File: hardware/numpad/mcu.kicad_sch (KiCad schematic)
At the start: 9 parts, among them U1 STM32L011F4Px

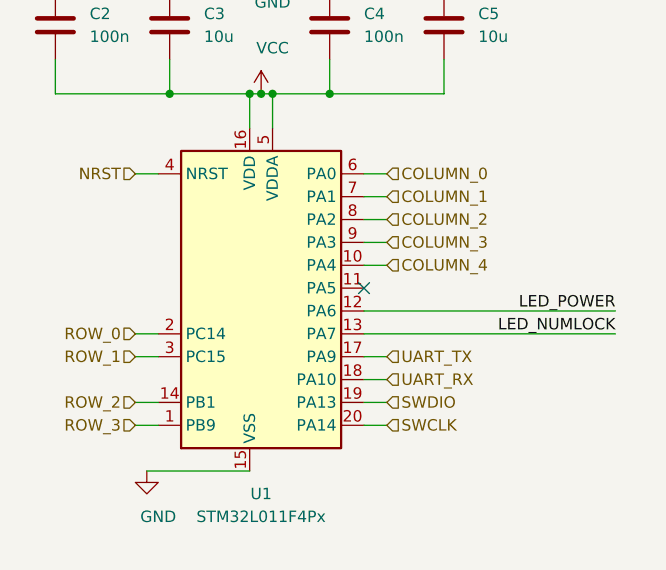
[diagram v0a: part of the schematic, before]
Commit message: Numpad: Fix labels of columns and rows of the key matrix
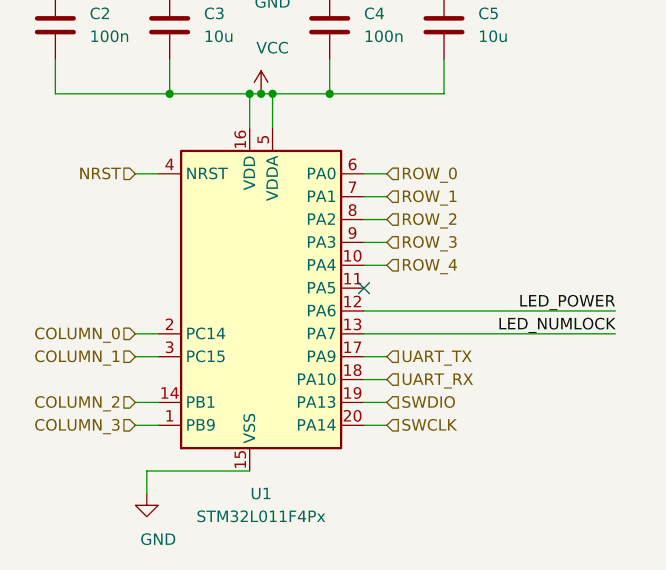
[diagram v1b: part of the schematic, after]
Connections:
- net COLUMN_0: now also U1.2 (PC14); no longer U1.6 (PA0)
- net COLUMN_1: now also U1.3 (PC15); no longer U1.7 (PA1)
- net COLUMN_2: now also U1.14 (PB1); no longer U1.8 (PA2)
- net COLUMN_3: now also U1.1 (PB9); no longer U1.9 (PA3)
- net ROW_0: now also U1.6 (PA0); no longer U1.2 (PC14)
- net ROW_1: now also U1.7 (PA1); no longer U1.3 (PC15)
- net ROW_2: now also U1.8 (PA2); no longer U1.14 (PB1)
- net ROW_3: now also U1.9 (PA3); no longer U1.1 (PB9)
- net COLUMN_4 renamed ROW_4
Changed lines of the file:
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@@
+    (stroke (width 0) (type solid) (color 0 0 0 0))
+  )
+  (wire (pts (xy 90.17 123.19) (xy 90.17 125.73))
     (stroke (width 0) (type solid) (color 0 0 0 0))
   )
@@
     (effects (font (size 1.27 1.27)) (justify right))
   )
-  (hierarchical_label "ROW_0" (shape input) (at 88.9 107.95 180)
+  (hierarchical_label "COLUMN_0" (shape input) (at 88.9 107.95 180)
     (effects (font (size 1.27 1.27)) (justify right))
   )
-  (hierarchical_label "ROW_1" (shape input) (at 88.9 110.49 180)
+  (hierarchical_label "COLUMN_1" (shape input) (at 88.9 110.49 180)
     (effects (font (size 1.27 1.27)) (justify right))
   )
-  (hierarchical_label "ROW_2" (shape input) (at 88.9 115.57 180)
+  (hierarchical_label "COLUMN_2" (shape input) (at 88.9 115.57 180)
     (effects (font (size 1.27 1.27)) (justify right))
   )
-  (hierarchical_label "ROW_3" (shape input) (at 88.9 118.11 180)
+  (hierarchical_label "COLUMN_3" (shape input) (at 88.9 118.11 180)
     (effects (font (size 1.27 1.27)) (justify right))
   )
-  (hierarchical_label "COLUMN_0" (shape input) (at 116.84 90.17 0)
+  (hierarchical_label "ROW_0" (shape input) (at 116.84 90.17 0)
     (effects (font (size 1.27 1.27)) (justify left))
   )
-  (hierarchical_label "COLUMN_1" (shape input) (at 116.84 92.71 0)
+  (hierarchical_label "ROW_1" (shape input) (at 116.84 92.71 0)
     (effects (font (size 1.27 1.27)) (justify left))
   )
-  (hierarchical_label "COLUMN_2" (shape input) (at 116.84 95.25 0)
+  (hierarchical_label "ROW_2" (shape input) (at 116.84 95.25 0)
     (effects (font (size 1.27 1.27)) (justify left))
   )
-  (hierarchical_label "COLUMN_3" (shape input) (at 116.84 97.79 0)
+  (hierarchical_label "ROW_3" (shape input) (at 116.84 97.79 0)
     (effects (font (size 1.27 1.27)) (justify left))
   )
-  (hierarchical_label "COLUMN_4" (shape input) (at 116.84 100.33 0)
+  (hierarchical_label "ROW_4" (shape input) (at 116.84 100.33 0)
     (effects (font (size 1.27 1.27)) (justify left))
   )
@@
     (pin "1")
   )
-  (symbol (lib_id "power:GND") (at 90.17 123.19 0) (unit 1)
+  (symbol (lib_id "power:GND") (at 90.17 125.73 0) (unit 1)
     (in_bom yes) (on_board yes)
-    (property "Reference" "#PWR0111" (id 0) (at 90.17 129.54 0)
+    (property "Reference" "#PWR0111" (id 0) (at 90.17 132.08 0)
       (effects (font (size 1.27 1.27)) hide)
     )
-    (property "Value" "GND" (id 1) (at 91.44 128.27 0))
-    (property "Footprint" "" (id 2) (at 90.17 123.19 0)
+    (property "Value" "GND" (id 1) (at 91.44 130.81 0))
+    (property "Footprint" "" (id 2) (at 90.17 125.73 0)
       (effects (font (size 1.27 1.27)) hide)
     )
-    (property "Datasheet" "" (id 3) (at 90.17 123.19 0)
+    (property "Datasheet" "" (id 3) (at 90.17 125.73 0)
       (effects (font (size 1.27 1.27)) hide)
     )

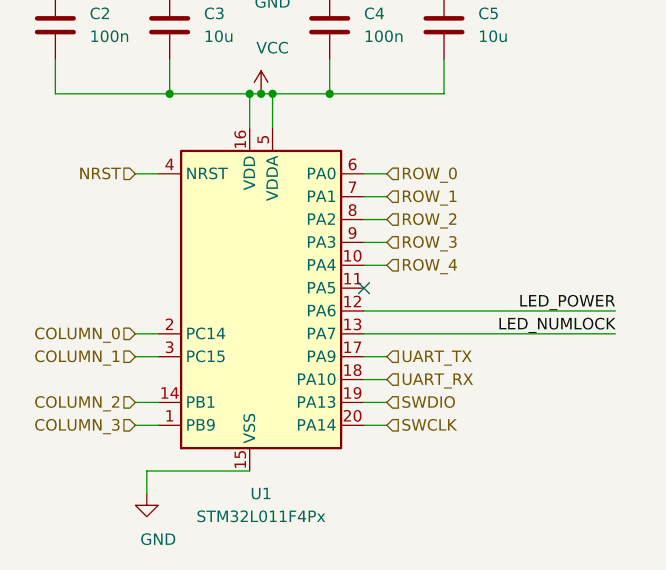
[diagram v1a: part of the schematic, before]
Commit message: Numpad: Create traces from the MCU to the keymatrix
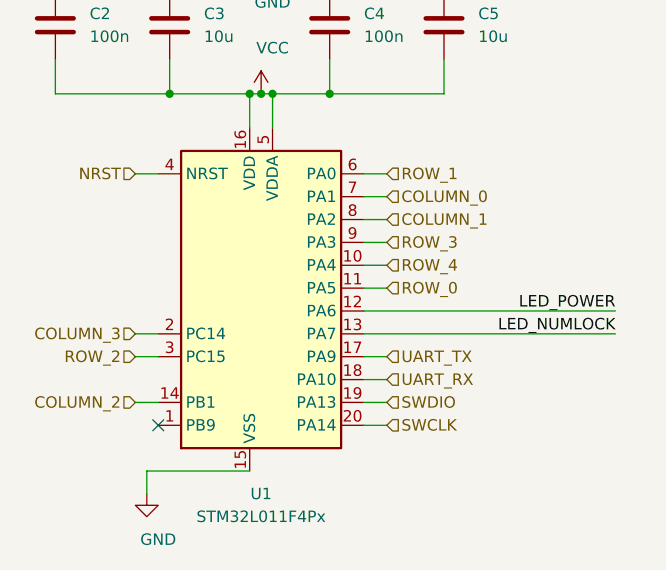
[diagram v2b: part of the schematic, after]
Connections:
- net COLUMN_0: now also U1.7 (PA1); no longer U1.2 (PC14)
- net COLUMN_1: now also U1.8 (PA2); no longer U1.3 (PC15)
- net COLUMN_3: now also U1.2 (PC14); no longer U1.1 (PB9)
- net ROW_0: now also U1.11 (PA5); no longer U1.6 (PA0)
- net ROW_1: now also U1.6 (PA0); no longer U1.7 (PA1)
- net ROW_2: now also U1.3 (PC15); no longer U1.8 (PA2)
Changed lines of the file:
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@@
   (junction (at 110.49 81.28) (diameter 0.9144) (color 0 0 0 0))
   (junction (at 234.95 66.04) (diameter 0.9144) (color 0 0 0 0))
-  (no_connect (at 114.3 102.87))
+  (no_connect (at 91.44 118.11))
   (wire (pts (xy 80.01 66.04) (xy 80.01 69.85))
     (stroke (width 0) (type solid) (color 0 0 0 0))
@@
   )
   (wire (pts (xy 88.9 115.57) (xy 91.44 115.57))
-    (stroke (width 0) (type solid) (color 0 0 0 0))
-  )
-  (wire (pts (xy 88.9 118.11) (xy 91.44 118.11))
     (stroke (width 0) (type solid) (color 0 0 0 0))
   )
@@
     (stroke (width 0) (type solid) (color 0 0 0 0))
   )
+  (wire (pts (xy 116.84 102.87) (xy 114.3 102.87))
+    (stroke (width 0) (type solid) (color 0 0 0 0))
+  )
   (wire (pts (xy 123.19 66.04) (xy 123.19 69.85))
     (stroke (width 0) (type solid) (color 0 0 0 0))
@@
     (effects (font (size 1.27 1.27)) (justify right))
   )
-  (hierarchical_label "COLUMN_0" (shape input) (at 88.9 107.95 180)
+  (hierarchical_label "COLUMN_3" (shape input) (at 88.9 107.95 180)
     (effects (font (size 1.27 1.27)) (justify right))
   )
-  (hierarchical_label "COLUMN_1" (shape input) (at 88.9 110.49 180)
+  (hierarchical_label "ROW_2" (shape input) (at 88.9 110.49 180)
     (effects (font (size 1.27 1.27)) (justify right))
   )
@@
     (effects (font (size 1.27 1.27)) (justify right))
   )
-  (hierarchical_label "COLUMN_3" (shape input) (at 88.9 118.11 180)
-    (effects (font (size 1.27 1.27)) (justify right))
-  )
-  (hierarchical_label "ROW_0" (shape input) (at 116.84 90.17 0)
+  (hierarchical_label "ROW_1" (shape input) (at 116.84 90.17 0)
     (effects (font (size 1.27 1.27)) (justify left))
   )
-  (hierarchical_label "ROW_1" (shape input) (at 116.84 92.71 0)
+  (hierarchical_label "COLUMN_0" (shape input) (at 116.84 92.71 0)
     (effects (font (size 1.27 1.27)) (justify left))
   )
-  (hierarchical_label "ROW_2" (shape input) (at 116.84 95.25 0)
+  (hierarchical_label "COLUMN_1" (shape input) (at 116.84 95.25 0)
     (effects (font (size 1.27 1.27)) (justify left))
   )
@@
     (effects (font (size 1.27 1.27)) (justify left))
   )
+  (hierarchical_label "ROW_0" (shape input) (at 116.84 102.87 0)
+    (effects (font (size 1.27 1.27)) (justify left))
+  )

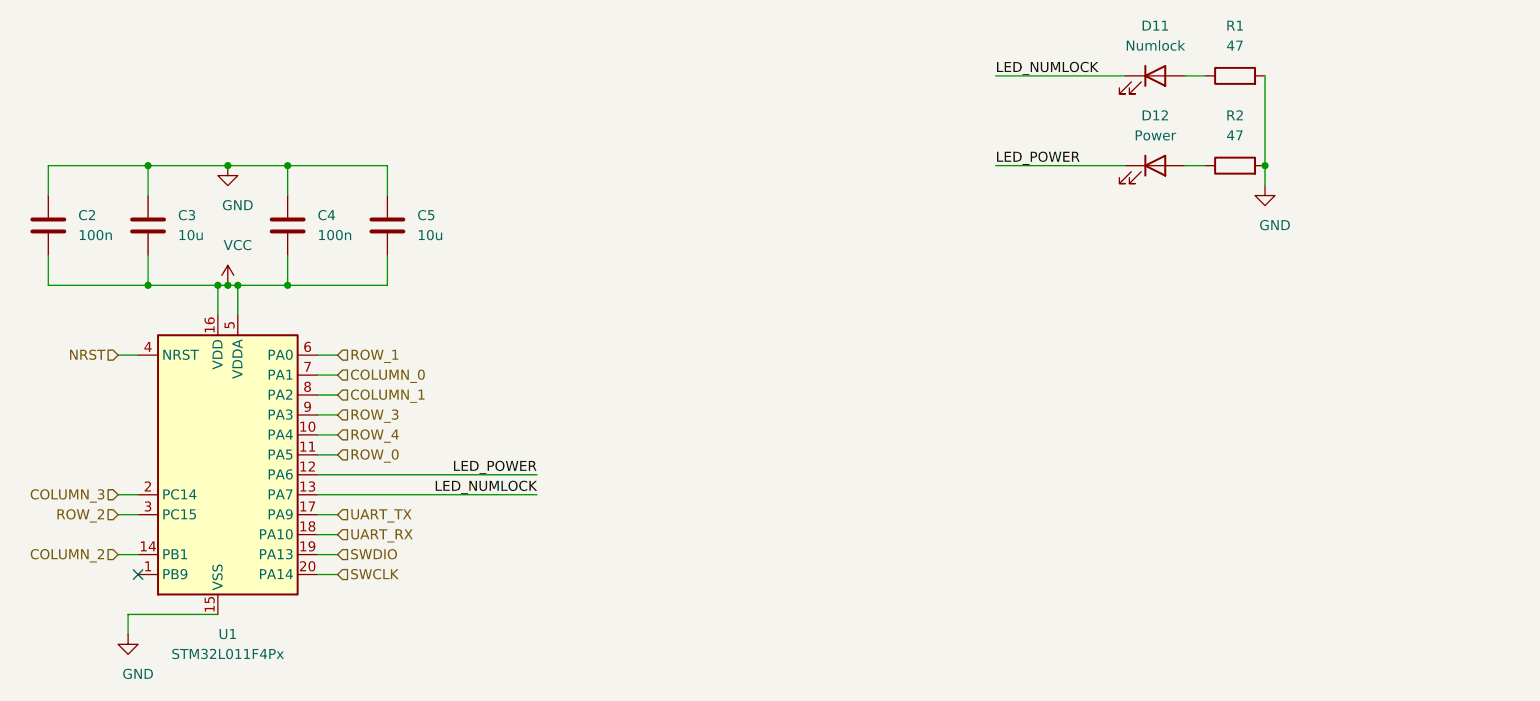
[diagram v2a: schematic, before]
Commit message: Numpad: Rework PCB layout
The Power-LED was eliminated and the Numpad-LED moved off the board.
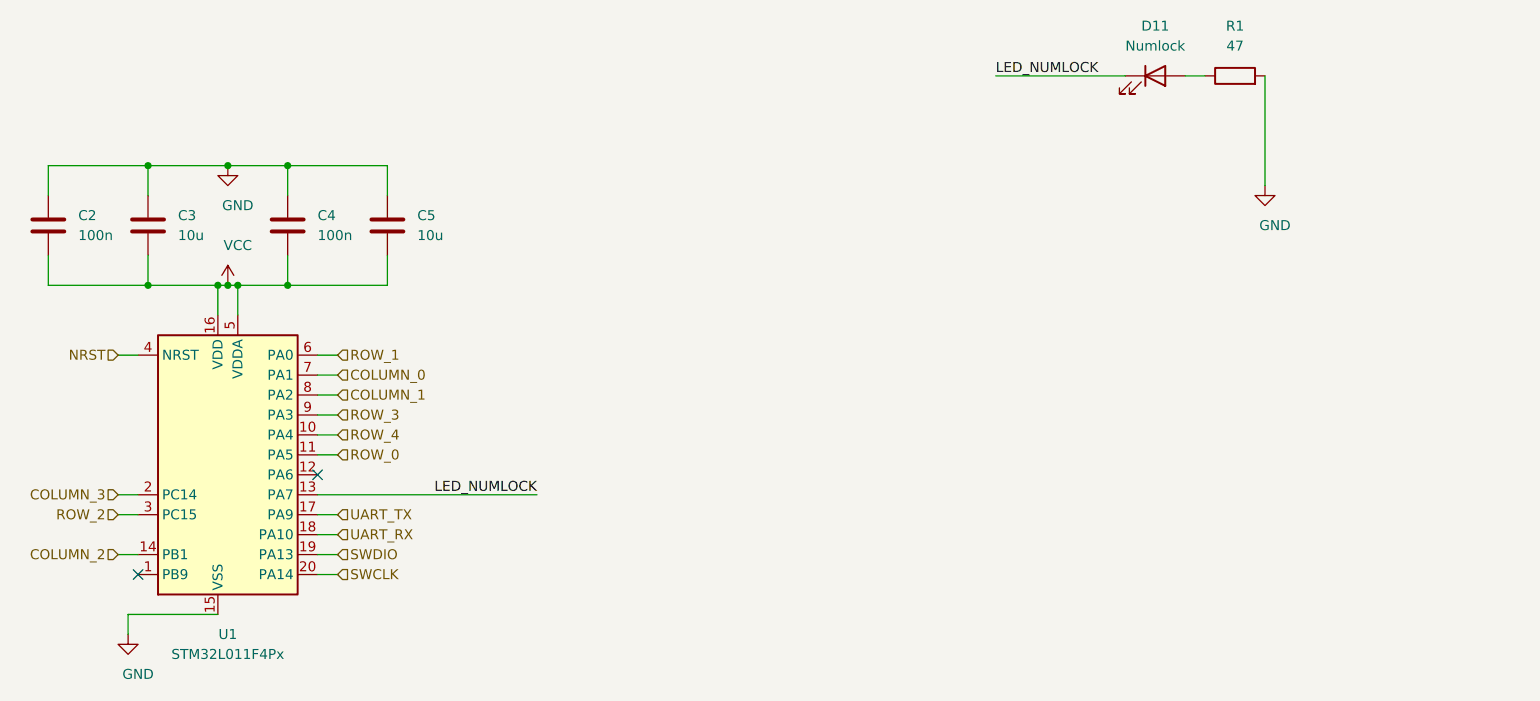
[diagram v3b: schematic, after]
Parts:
- removed D12: Power, Diode_SMD:D_0603_1608Metric_Pad1.05x0.95mm_HandSolder, symbol Device:LED
- removed R2: 47, Resistor_SMD:R_0603_1608Metric_Pad0.98x0.95mm_HandSolder, symbol Device:R
- D11: footprint Diode_SMD:D_0603_1608Metric_Pad1.05x0.95mm_HandSolder -> Diode_THT:D_DO-34_SOD68_P2.54mm_Vertical_AnodeUp
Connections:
- net LED_POWER: no longer names the net of U1.12 (PA6)
- no-connect marks 1 -> 2
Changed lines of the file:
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@@
   (junction (at 110.49 66.04) (diameter 0.9144) (color 0 0 0 0))
   (junction (at 110.49 81.28) (diameter 0.9144) (color 0 0 0 0))
-  (junction (at 234.95 66.04) (diameter 0.9144) (color 0 0 0 0))
   (no_connect (at 91.44 118.11))
+  (no_connect (at 114.3 105.41))
   (wire (pts (xy 80.01 66.04) (xy 80.01 69.85))
     (stroke (width 0) (type solid) (color 0 0 0 0))
@@
     (stroke (width 0) (type solid) (color 0 0 0 0))
   )
-  (wire (pts (xy 142.24 105.41) (xy 114.3 105.41))
-    (stroke (width 0) (type solid) (color 0 0 0 0))
-  )
   (wire (pts (xy 142.24 107.95) (xy 114.3 107.95))
     (stroke (width 0) (type solid) (color 0 0 0 0))
@@
     (stroke (width 0) (type solid) (color 0 0 0 0))
   )
-  (wire (pts (xy 200.66 66.04) (xy 217.17 66.04))
-    (stroke (width 0) (type solid) (color 0 0 0 0))
-  )
   (wire (pts (xy 224.79 54.61) (xy 227.33 54.61))
     (stroke (width 0) (type solid) (color 0 0 0 0))
   )
-  (wire (pts (xy 224.79 66.04) (xy 227.33 66.04))
-    (stroke (width 0) (type solid) (color 0 0 0 0))
-  )
-  (wire (pts (xy 234.95 54.61) (xy 234.95 66.04))
-    (stroke (width 0) (type solid) (color 0 0 0 0))
-  )
-  (wire (pts (xy 234.95 66.04) (xy 234.95 68.58))
-    (stroke (width 0) (type solid) (color 0 0 0 0))
-  )
-  (label "LED_POWER" (at 142.24 105.41 180)
-    (effects (font (size 1.27 1.27)) (justify right bottom))
+  (wire (pts (xy 234.95 54.61) (xy 234.95 68.58))
+    (stroke (width 0) (type solid) (color 0 0 0 0))
   )
   (label "LED_NUMLOCK" (at 142.24 107.95 180)
@@
   )
   (label "LED_NUMLOCK" (at 200.66 54.61 0)
-    (effects (font (size 1.27 1.27)) (justify left bottom))
-  )
-  (label "LED_POWER" (at 200.66 66.04 0)
     (effects (font (size 1.27 1.27)) (justify left bottom))
   )
@@
     (pin "2")
   )
-  (symbol (lib_id "Device:R") (at 231.14 66.04 90) (unit 1)
-    (in_bom yes) (on_board yes)
-    (property "Reference" "R2" (id 0) (at 231.14 59.69 90))
-    (property "Value" "47" (id 1) (at 231.14 62.23 90))
-    (property "Footprint" "Resistor_SMD:R_0603_1608Metric_Pad0.98x0.95mm_HandSolder" (id 2) (at 231.14 67.818 90)
-      (effects (font (size 1.27 1.27)) hide)
-    )
-    (property "Datasheet" "~" (id 3) (at 231.14 66.04 0)
-      (effects (font (size 1.27 1.27)) hide)
-    )
-    (pin "1")
-    (pin "2")
-  )
   (symbol (lib_id "Device:LED") (at 220.98 54.61 0) (unit 1)
     (in_bom yes) (on_board yes)
     (property "Reference" "D11" (id 0) (at 220.98 48.26 0))
     (property "Value" "Numlock" (id 1) (at 220.98 50.8 0))
-    (property "Footprint" "Diode_SMD:D_0603_1608Metric_Pad1.05x0.95mm_HandSolder" (id 2) (at 220.98 54.61 0)
+    (property "Footprint" "Diode_THT:D_DO-34_SOD68_P2.54mm_Vertical_AnodeUp" (id 2) (at 220.98 54.61 0)
       (effects (font (size 1.27 1.27)) hide)
     )
@@
       (effects (font (size 1.27 1.27)) hide)
     )
-    (pin "1")
-    (pin "2")
-  )
-  (symbol (lib_id "Device:LED") (at 220.98 66.04 0) (unit 1)
-    (in_bom yes) (on_board yes)
-    (property "Reference" "D12" (id 0) (at 220.98 59.69 0))
-    (property "Value" "Power" (id 1) (at 220.98 62.23 0))
-    (property "Footprint" "Diode_SMD:D_0603_1608Metric_Pad1.05x0.95mm_HandSolder" (id 2) (at 220.98 66.04 0)
-      (effects (font (size 1.27 1.27)) hide)
-    )
-    (property "Datasheet" "~" (id 3) (at 220.98 66.04 0)
-      (effects (font (size 1.27 1.27)) hide)
-    )
